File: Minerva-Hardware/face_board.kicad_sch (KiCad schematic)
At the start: 1 part, among them U3 RP2040

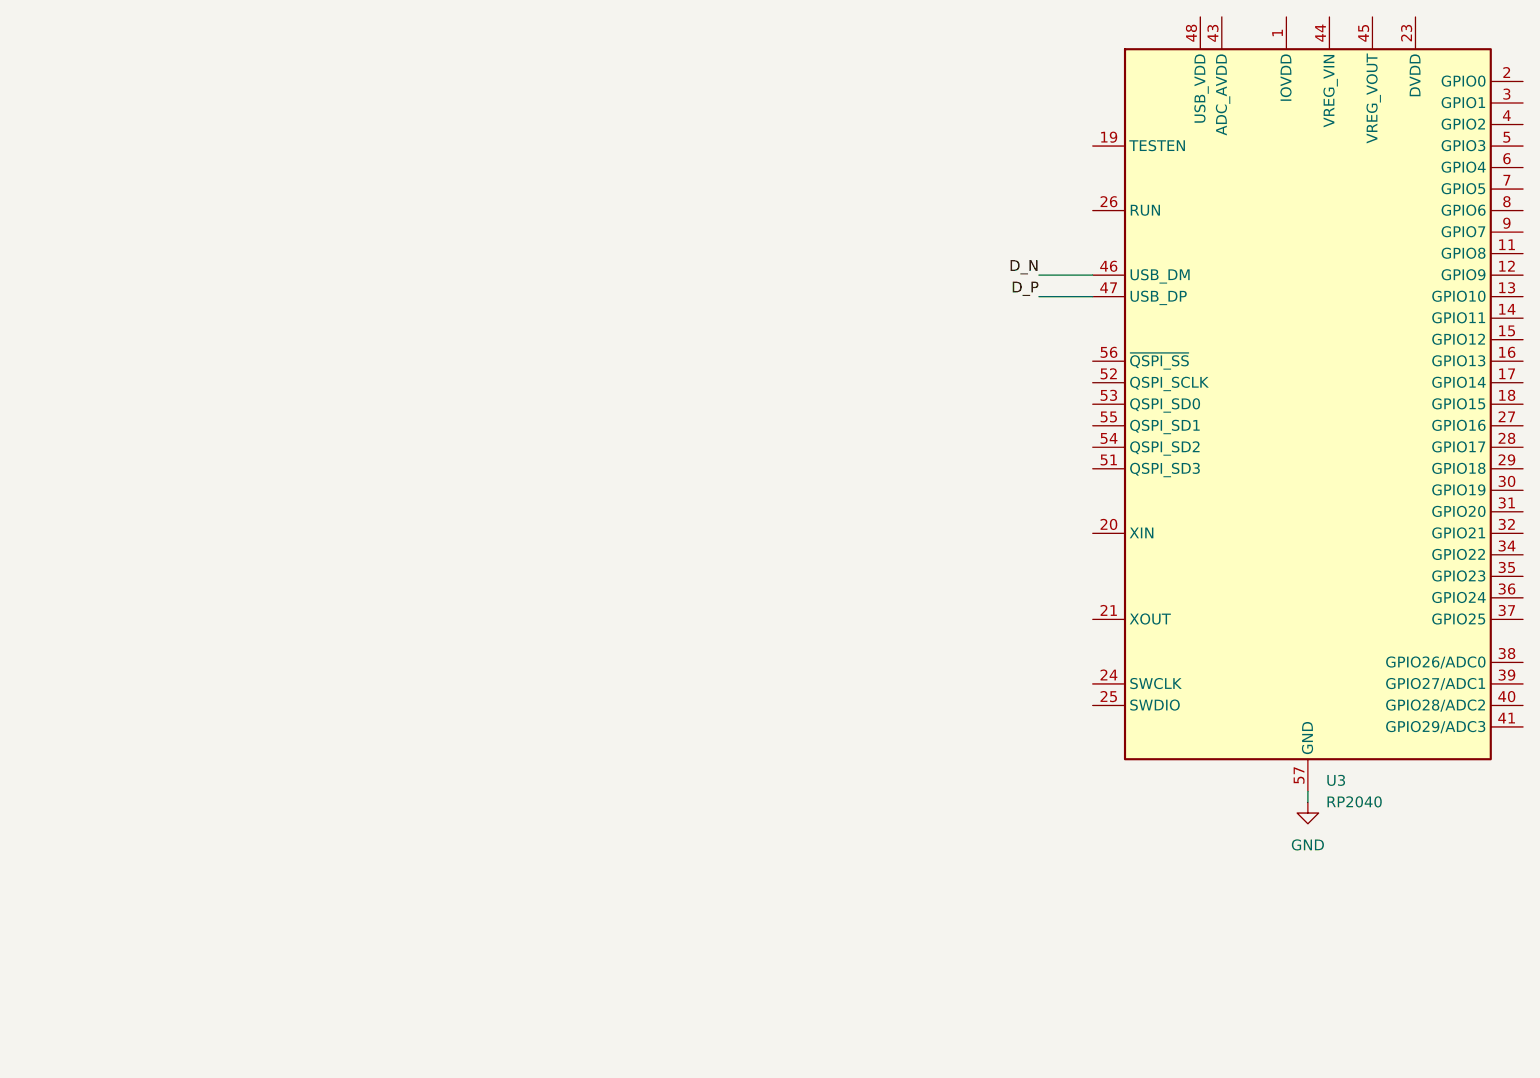
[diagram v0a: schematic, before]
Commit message: Redid the BQ powerpath unit
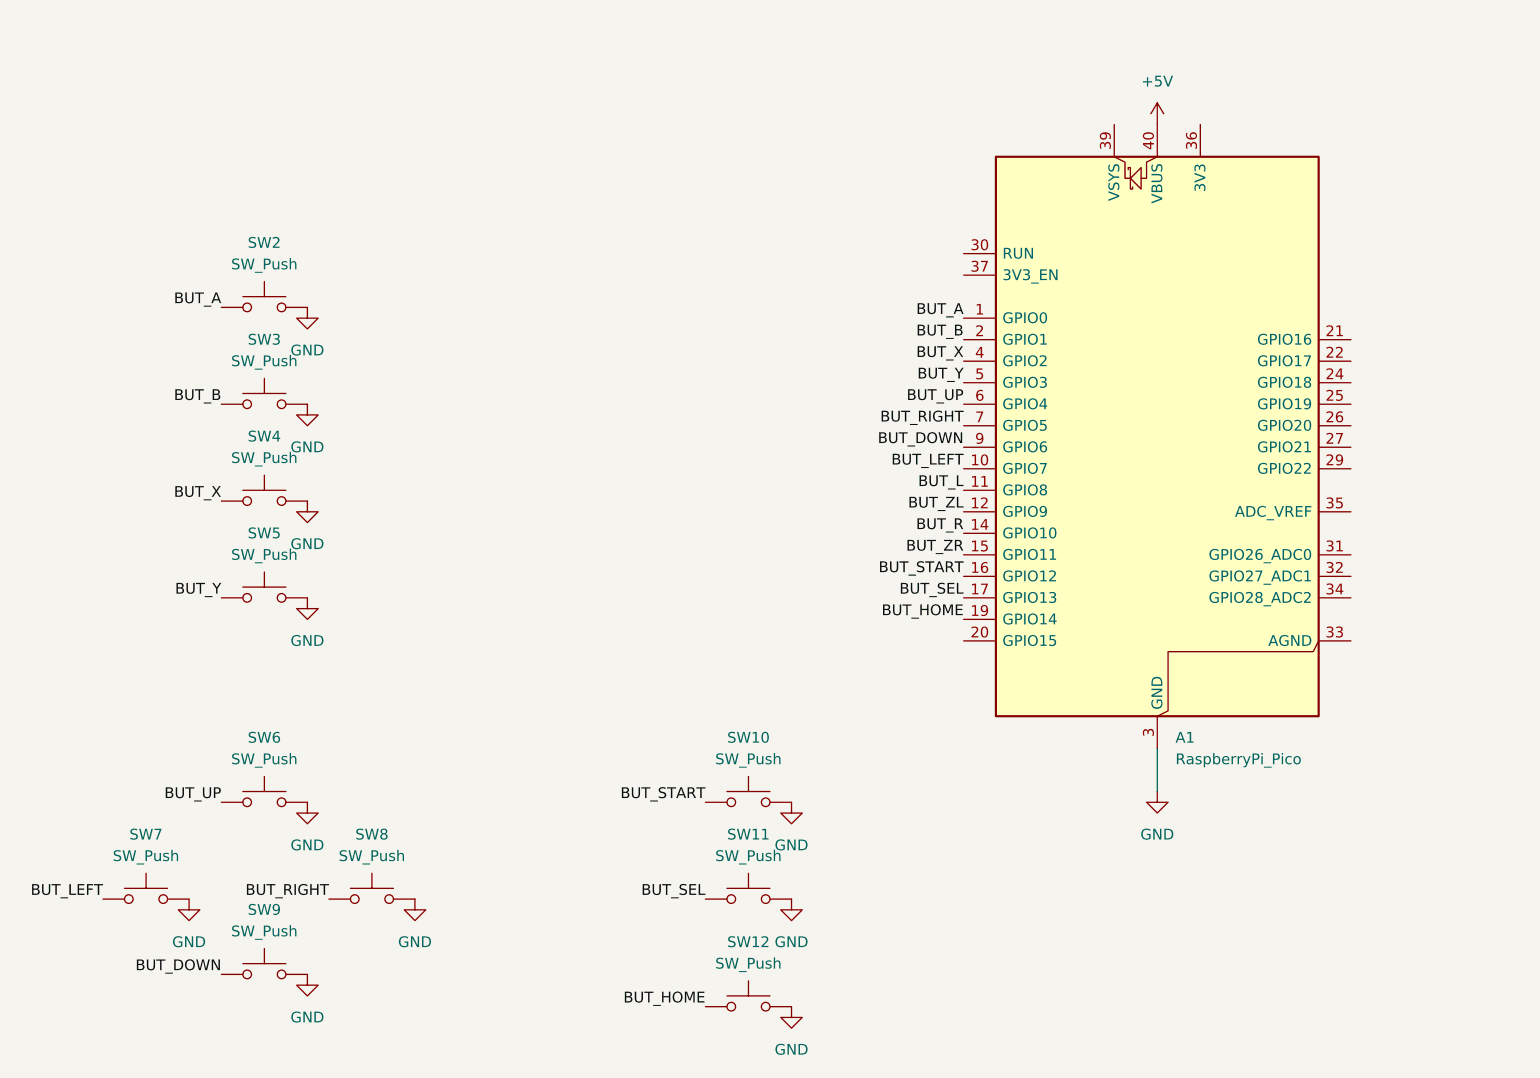
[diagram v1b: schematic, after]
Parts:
- removed U3: RP2040, Package_DFN_QFN:QFN-56-1EP_7x7mm_P0.4mm_EP3.2x3.2mm, symbol MCU_RaspberryPi:RP2040
- added A1: RaspberryPi_Pico, Module:RaspberryPi_Pico_Common_Unspecified, symbol MCU_Module:RaspberryPi_Pico
- added SW10, SW11, SW12, SW2, SW3, SW4, SW5, SW6, SW7, SW8, SW9: SW_Push, symbol Switch:SW_Push
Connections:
- net GND: now also A1.13 (GND), A1.18 (GND), A1.23 (GND), A1.28 (GND), A1.3 (GND), A1.38 (GND), A1.8 (GND), SW10.2, SW11.2, SW12.2, SW2.2, SW3.2, SW4.2, SW5.2, SW6.2, SW7.2, SW8.2, SW9.2
- new net +5V: A1.40 (VBUS)
- new net BUT_A: A1.1 (GPIO0), SW2.1
- new net BUT_B: A1.2 (GPIO1), SW3.1
- new net BUT_DOWN: A1.9 (GPIO6), SW9.1
- new net BUT_HOME: A1.19 (GPIO14), SW12.1
- new net BUT_L: A1.11 (GPIO8)
- new net BUT_LEFT: A1.10 (GPIO7), SW7.1
- new net BUT_R: A1.14 (GPIO10)
- new net BUT_RIGHT: A1.7 (GPIO5), SW8.1
- new net BUT_SEL: A1.17 (GPIO13), SW11.1
- new net BUT_START: A1.16 (GPIO12), SW10.1
- new net BUT_UP: A1.6 (GPIO4), SW6.1
- new net BUT_X: A1.4 (GPIO2), SW4.1
- new net BUT_Y: A1.5 (GPIO3), SW5.1
- new net BUT_ZL: A1.12 (GPIO9)
- new net BUT_ZR: A1.15 (GPIO11)

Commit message: working on pcb more
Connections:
- no-connect marks 0 -> 1
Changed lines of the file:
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@@
 	(generator_version "10.0")
 	(paper "A4")
+	(no_connect
+		(at 201.93 114.3)
+	)
 	(wire
 		(pts
-			(xy 179.07 127) (xy 179.07 132.08)
+			(xy 179.07 127) (xy 179.07 128.27)
 		)
 		(stroke
@@
 	(symbol
 		(lib_id "power:GND")
-		(at 179.07 132.08 0)
+		(at 179.07 128.27 0)
 		(unit 1)
 		(body_style 1)
@@
 		(fields_autoplaced yes)
 		(property "Reference" "#PWR019"
-			(at 179.07 138.43 0)
+			(at 179.07 134.62 0)
 			(hide yes)
 			(show_name no)
@@
 		)
 		(property "Value" "GND"
-			(at 179.07 137.16 0)
+			(at 179.07 133.35 0)
 			(show_name no)
 			(do_not_autoplace no)
@@
 		)
 		(property "Footprint" ""
-			(at 179.07 132.08 0)
+			(at 179.07 128.27 0)
 			(hide yes)
 			(show_name no)
@@
 		)
 		(property "Datasheet" ""
-			(at 179.07 132.08 0)
+			(at 179.07 128.27 0)
 			(hide yes)
 			(show_name no)
@@
 		)
 		(property "Description" "Power symbol creates a global label with name \"GND\" , ground"
-			(at 179.07 132.08 0)
-			(hide yes)
-			(show_name no)
+			(at 179.07 128.27 0)
+			(hide yes)
+			(show_name no)
